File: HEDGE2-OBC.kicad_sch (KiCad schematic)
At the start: 31 parts, among them J1 MMBX-S50-0-18, J2 SQT-110-01-L-D, J3 SMA-J-P-X-RA-TH1, U1 ADP7158ARDZ-3.3-R7

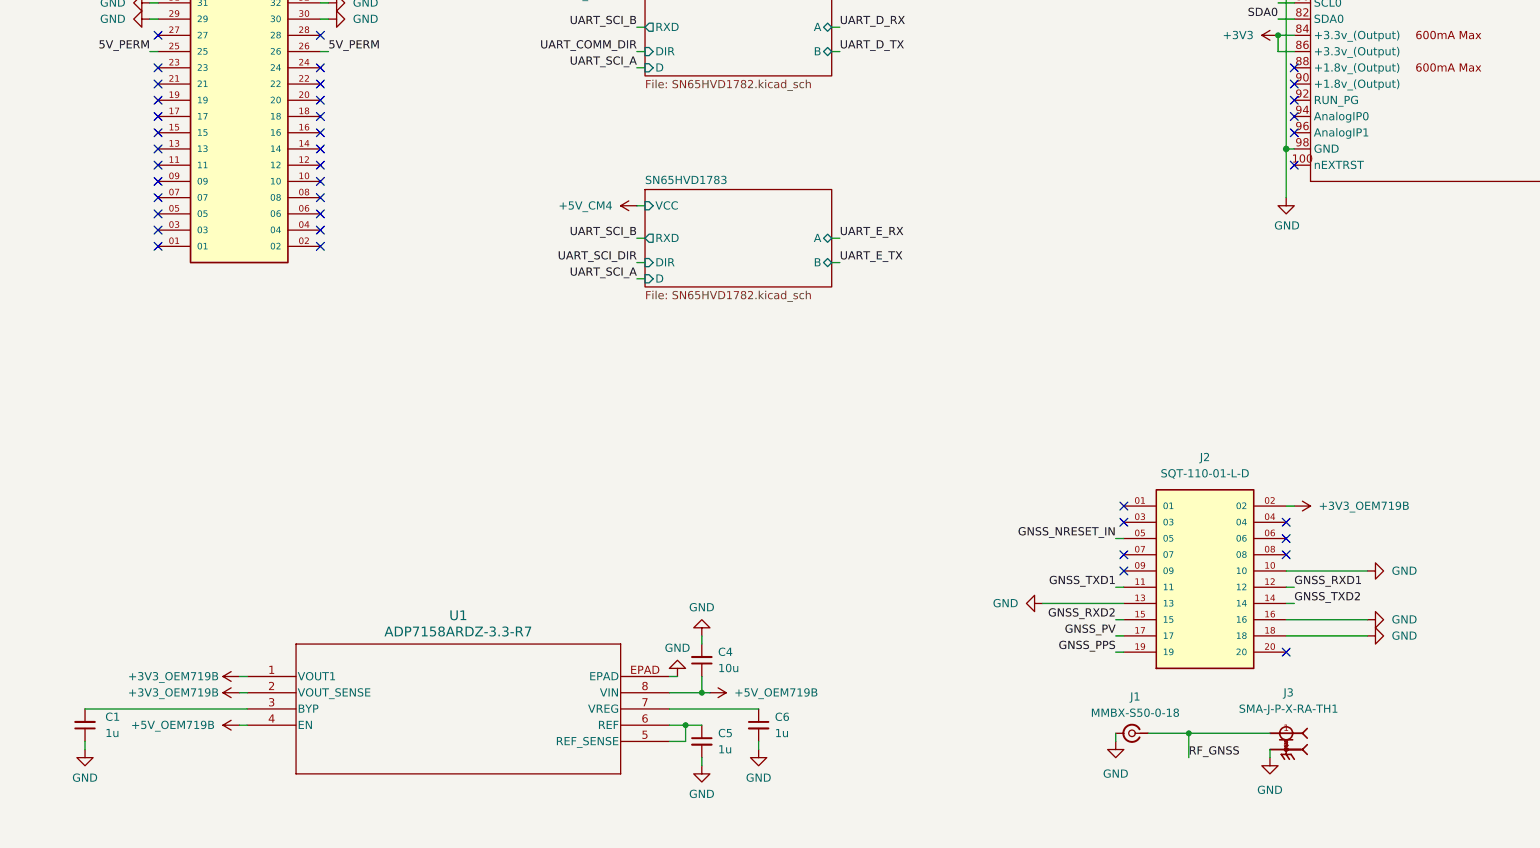
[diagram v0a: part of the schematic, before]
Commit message: Rework Novatel OEM719B symbol and footprint
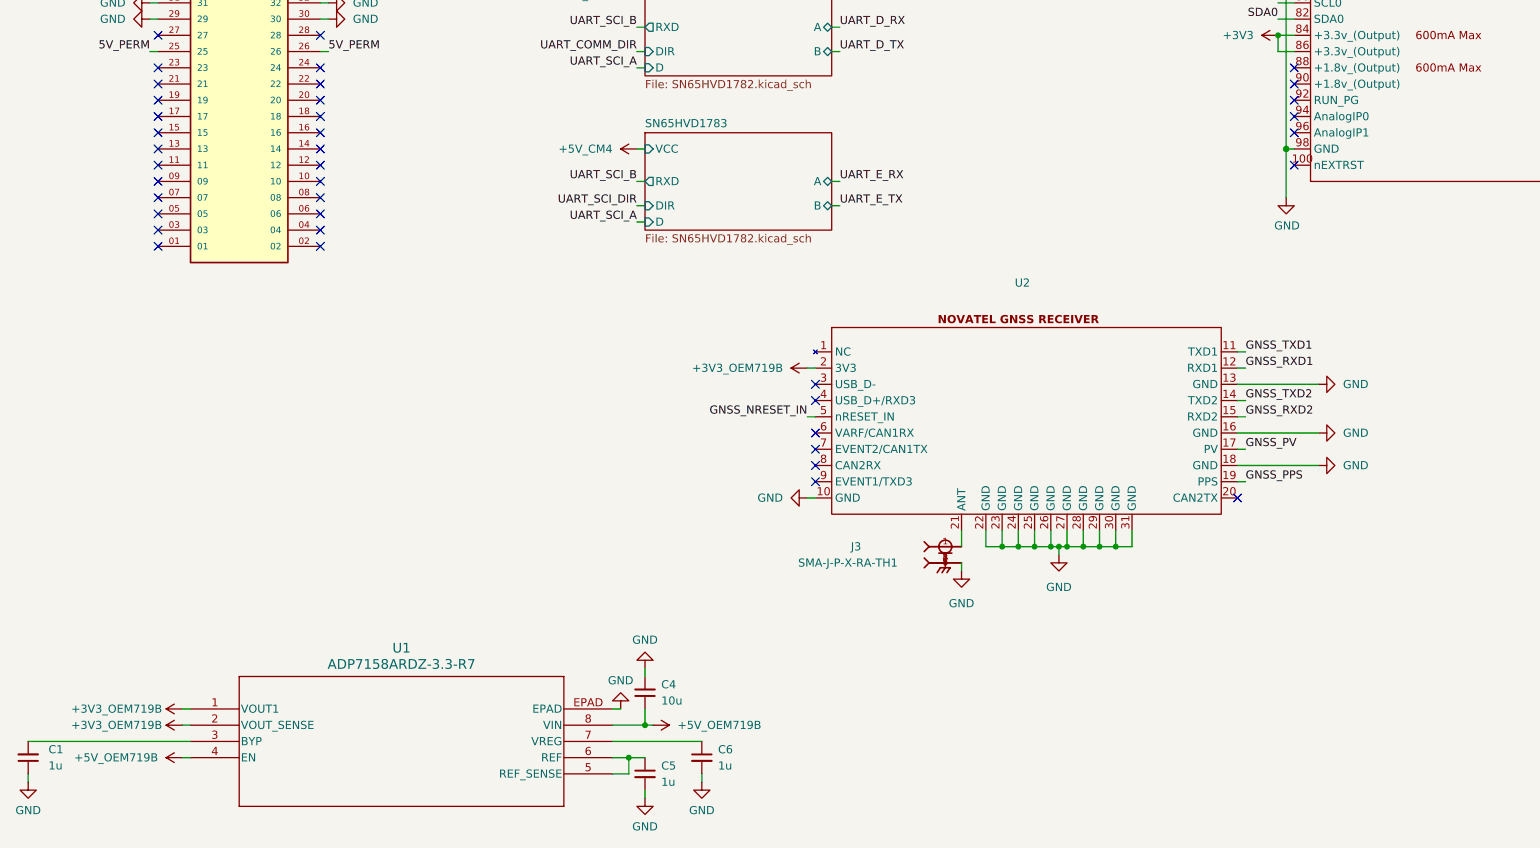
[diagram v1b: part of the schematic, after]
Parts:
- removed J1: MMBX-S50-0-18, Novatel:MMBX-S50-0-18, symbol Novatel:MMBX-S50-0-18
- removed J2: SQT-110-01-L-D, SQT-110-01-L-D:SAMTEC_SQT-110-01-L-D, symbol SQT-110-01-L-D:SQT-110-01-L-D
- added U2: ~, OEM719B:OEM719B, symbol OEM719B:NOVATEL_OEM719
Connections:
- net +3V3_OEM719B: now also U2.2 (3V3)
- net GND: now also U2.10 (GND), U2.13 (GND), U2.16 (GND), U2.18 (GND), U2.22 (GND), U2.23 (GND), U2.24 (GND), U2.25 (GND), U2.26 (GND), U2.27 (GND), U2.28 (GND), U2.29 (GND), U2.30 (GND), U2.31 (GND)
- net GNSS_NRESET_IN: now also U2.5 (nRESET_IN)
- net GNSS_PPS: now also U2.19 (PPS)
- net GNSS_PV: now also U2.17 (PV)
- net GNSS_RXD1: now also U2.12 (RXD1)
- net GNSS_RXD2: now also U2.15 (RXD2)
- net GNSS_TXD1: now also U2.11 (TXD1)
- net GNSS_TXD2: now also U2.14 (TXD2)
- net RF_GNSS: no longer names the net of J3.1
- net RF_GNSS: now also U2.21 (ANT)
- no-connect marks 205 -> 204
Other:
- moved on the sheet: C1, C4, C5, C6, J3, U1

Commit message: Layout PCB; update footprints with 3D models
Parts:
- added C7, C8: 0u1, Capacitor_SMD:C_0805_2012Metric, symbol Device:C_Small
- added R20, R21: 4k7, Resistor_SMD:R_0805_2012Metric, symbol Device:R_Small_US
- added R5: 10k, Resistor_SMD:R_0805_2012Metric, symbol Device:R_Small_US
- added U3: TXS0102QDCURQ1, TXS0102QDCURQ1:SOP50P310X90-8N, symbol TXS0102QDCURQ1:TXS0102QDCURQ1
- renumbered J3 to J1, R9 to R10, R10 to R11, R5 to R6, R6 to R7, R7 to R8, R8 to R9
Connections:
- net +3V3: now also C7.2, U3.3 (VCCA)
- net +5V_MPU: now also C8.1, R20.2, R21.2, U3.7 (VCCB)
- net GND: now also C7.1, C8.2, R5.1, U3.2 (GND)
- net SCL0 renamed SCL0_3V3
- net SCL0_3V3: now also U3.5 (A1)
- net SDA0 renamed SDA0_3V3
- net SDA0_3V3: now also U3.4 (A2)
- new net I2C_EN: R5.2, U3.6 (OE)
- new net SCL0_5V: R20.1, U3.1 (B2)
- new net SDA0_5V: R21.1, U3.8 (B1)
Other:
- moved on the sheet: D1, D2, J1, R10, R11, R8, R9, U2

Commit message: Continue PCB layout
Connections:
- net CAN_A_S: now also Module1.49 (GPIO18); no longer Module1.29 (GPIO16)
- net CAN_B_S: now also Module1.37 (GPIO7); no longer Module1.58 (GPIO2)
- net GNSS_NRESET_IN: now also Module1.48 (GPIO27); no longer Module1.38 (GPIO11)
- net I2C_EN: now also Module1.30 (GPIO6)
- net UART_COMM_DIR: now also Module1.41 (GPIO25); no longer Module1.47 (GPIO23)
- net UART_SCI_A: no longer Module1.39 (GPIO8)
- net UART_SCI_B: no longer Module1.40 (GPIO9)
- net UART_SCI_DIR: now also Module1.26 (GPIO19); no longer Module1.45 (GPIO24)
- new net UART_COMM_A: Module1.39 (GPIO8)
- new net UART_COMM_B: Module1.40 (GPIO9)
- no-connect marks 204 -> 203
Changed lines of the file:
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@@
 	)
 	(no_connect
+		(at 276.86 90.17)
+	)
+	(no_connect
 		(at 38.1 138.43)
 	)
@@
 	)
 	(no_connect
-		(at 215.9 92.71)
-	)
-	(no_connect
 		(at 215.9 110.49)
 	)
@@
 	)
 	(no_connect
-		(at 276.86 95.25)
-	)
-	(no_connect
 		(at 330.2 69.85)
 	)
@@
 	)
 	(no_connect
-		(at 276.86 85.09)
+		(at 276.86 92.71)
 	)
 	(no_connect
@@
 	)
 	(no_connect
+		(at 215.9 80.01)
+	)
+	(no_connect
 		(at 276.86 57.15)
 	)
@@
 	)
 	(no_connect
+		(at 215.9 105.41)
+	)
+	(no_connect
 		(at 38.1 163.83)
 	)
@@
 	)
 	(no_connect
-		(at 215.9 64.77)
-	)
-	(no_connect
 		(at 276.86 156.21)
 	)
@@
 	)
 	(no_connect
+		(at 276.86 69.85)
+	)
+	(no_connect
 		(at 215.9 143.51)
 	)
@@
 	)
 	(no_connect
-		(at 215.9 69.85)
-	)
-	(no_connect
 		(at 330.2 52.07)
 	)
@@
 	)
 	(no_connect
-		(at 276.86 80.01)
-	)
-	(no_connect
 		(at 215.9 46.99)
 	)
@@
 	(wire
 		(pts
+			(xy 213.36 69.85) (xy 215.9 69.85)
+		)
+		(stroke
+			(width 0)
+			(type default)
+		)
+	)
+	(wire
+		(pts
 			(xy 36.83 133.35) (xy 38.1 133.35)
 		)
@@
 	(wire
 		(pts
-			(xy 276.86 90.17) (xy 279.4 90.17)
+			(xy 215.9 64.77) (xy 213.36 64.77)
 		)
 		(stroke
@@
 	(wire
 		(pts
+			(xy 276.86 80.01) (xy 279.4 80.01)
+		)
+		(stroke
+			(width 0)
+			(type default)
+		)
+	)
+	(wire
+		(pts
 			(xy 213.36 100.33) (xy 215.9 100.33)
 		)
@@
 	(wire
 		(pts
+			(xy 276.86 95.25) (xy 279.4 95.25)
+		)
+		(stroke
+			(width 0)
+			(type default)
+		)
+	)
+	(wire
+		(pts
 			(xy 109.22 243.84) (xy 110.49 243.84)
 		)
@@
 	(wire
 		(pts
-			(xy 276.86 92.71) (xy 279.4 92.71)
+			(xy 276.86 85.09) (xy 279.4 85.09)
 		)
 		(stroke
@@
 	(wire
 		(pts
-			(xy 276.86 69.85) (xy 279.4 69.85)
-		)
-		(stroke
-			(width 0)
-			(type solid)
-		)
-	)
-	(wire
-		(pts
 			(xy 327.66 57.15) (xy 327.66 64.77)
 		)
@@
 	(wire
 		(pts
-			(xy 213.36 80.01) (xy 215.9 80.01)
+			(xy 213.36 92.71) (xy 215.9 92.71)
 		)
 		(stroke
@@
 	(wire
 		(pts
-			(xy 213.36 105.41) (xy 215.9 105.41)
-		)
-		(stroke
-			(width 0)
-			(type default)
-		)
-	)
-	(wire
-		(pts
 			(xy 327.66 110.49) (xy 327.66 118.11)
 		)
@@
 				)
 			)
-			(table_cell "GNSS_TXD"
+			(table_cell "GNSS_TXD2"
 				(exclude_from_sim no)
 				(at 264.16 232.41 0)
@@
 				)
 			)
-			(table_cell "GNSS_RXD"
+			(table_cell "GNSS_RXD2"
 				(exclude_from_sim no)
 				(at 264.16 234.95 0)
@@
 		)
 	)
-	(label "UART_SCI_A"
+	(label "UART_COMM_A"
 		(at 279.4 82.55 0)
 		(effects
@@
 		)
 	)
+	(label "I2C_EN"
+		(at 213.36 69.85 180)
+		(effects
+			(font
+				(size 1.27 1.27)
+			)
+			(justify right bottom)
+		)
+	)
 	(label "UART_COMM_DIR"
 		(at 113.03 140.97 180)
@@
 		)
 	)
-	(label "UART_SCI_B"
+	(label "UART_COMM_B"
 		(at 113.03 137.16 180)
 		(effects
@@
 	)
 	(label "CAN_A_S"
-		(at 279.4 69.85 0)
+		(at 279.4 95.25 0)
 		(effects
 			(font
@@
 	)
 	(label "GNSS_NRESET_IN"
-		(at 213.36 80.01 180)
+		(at 213.36 92.71 180)
 		(effects
 			(font
@@
 	)
 	(label "UART_SCI_DIR"
-		(at 279.4 90.17 0)
+		(at 213.36 64.77 180)
 		(effects
 			(font
 				(size 1.27 1.27)
 			)
-			(justify left bottom)
+			(justify right bottom)
 		)
 	)
@@
 	)
 	(label "UART_COMM_DIR"
-		(at 279.4 92.71 0)
+		(at 279.4 85.09 0)
 		(effects
 			(font
@@
 		)
 	)
-	(label "UART_SCI_B"
+	(label "UART_COMM_B"
 		(at 213.36 82.55 180)
 		(effects
@@
 	)
 	(label "CAN_B_S"
-		(at 213.36 105.41 180)
+		(at 279.4 80.01 0)
 		(effects
 			(font
 				(size 1.27 1.27)
 			)
-			(justify right bottom)
+			(justify left bottom)
 		)
 	)
@@
 		)
 	)
-	(label "UART_SCI_A"
+	(label "UART_COMM_A"
 		(at 113.03 143.51 180)
 		(effects

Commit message: Continue layout
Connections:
- net +5V_CM4: now also C8.1, R20.2, R21.2, U3.7 (VCCB)
- net +5V_MPU: no longer C8.1, R20.2, R21.2, U3.7 (VCCB)

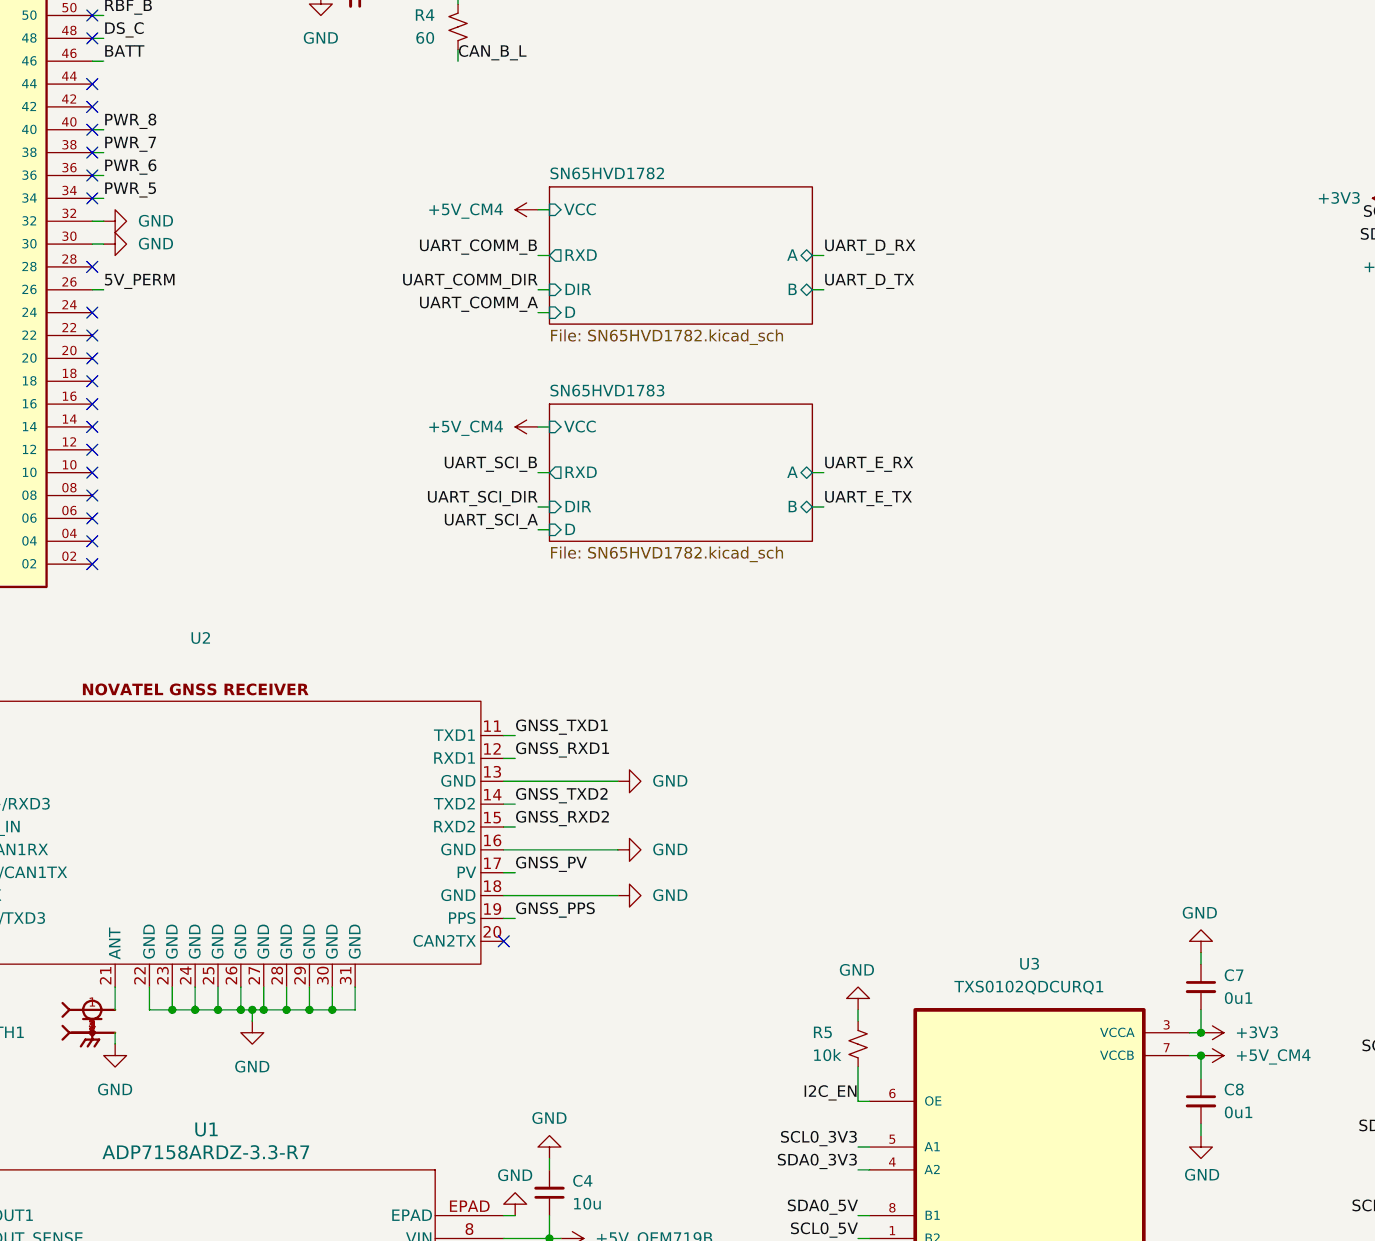
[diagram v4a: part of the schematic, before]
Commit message: Fix MMBX footprint; resolve ERC/DRC
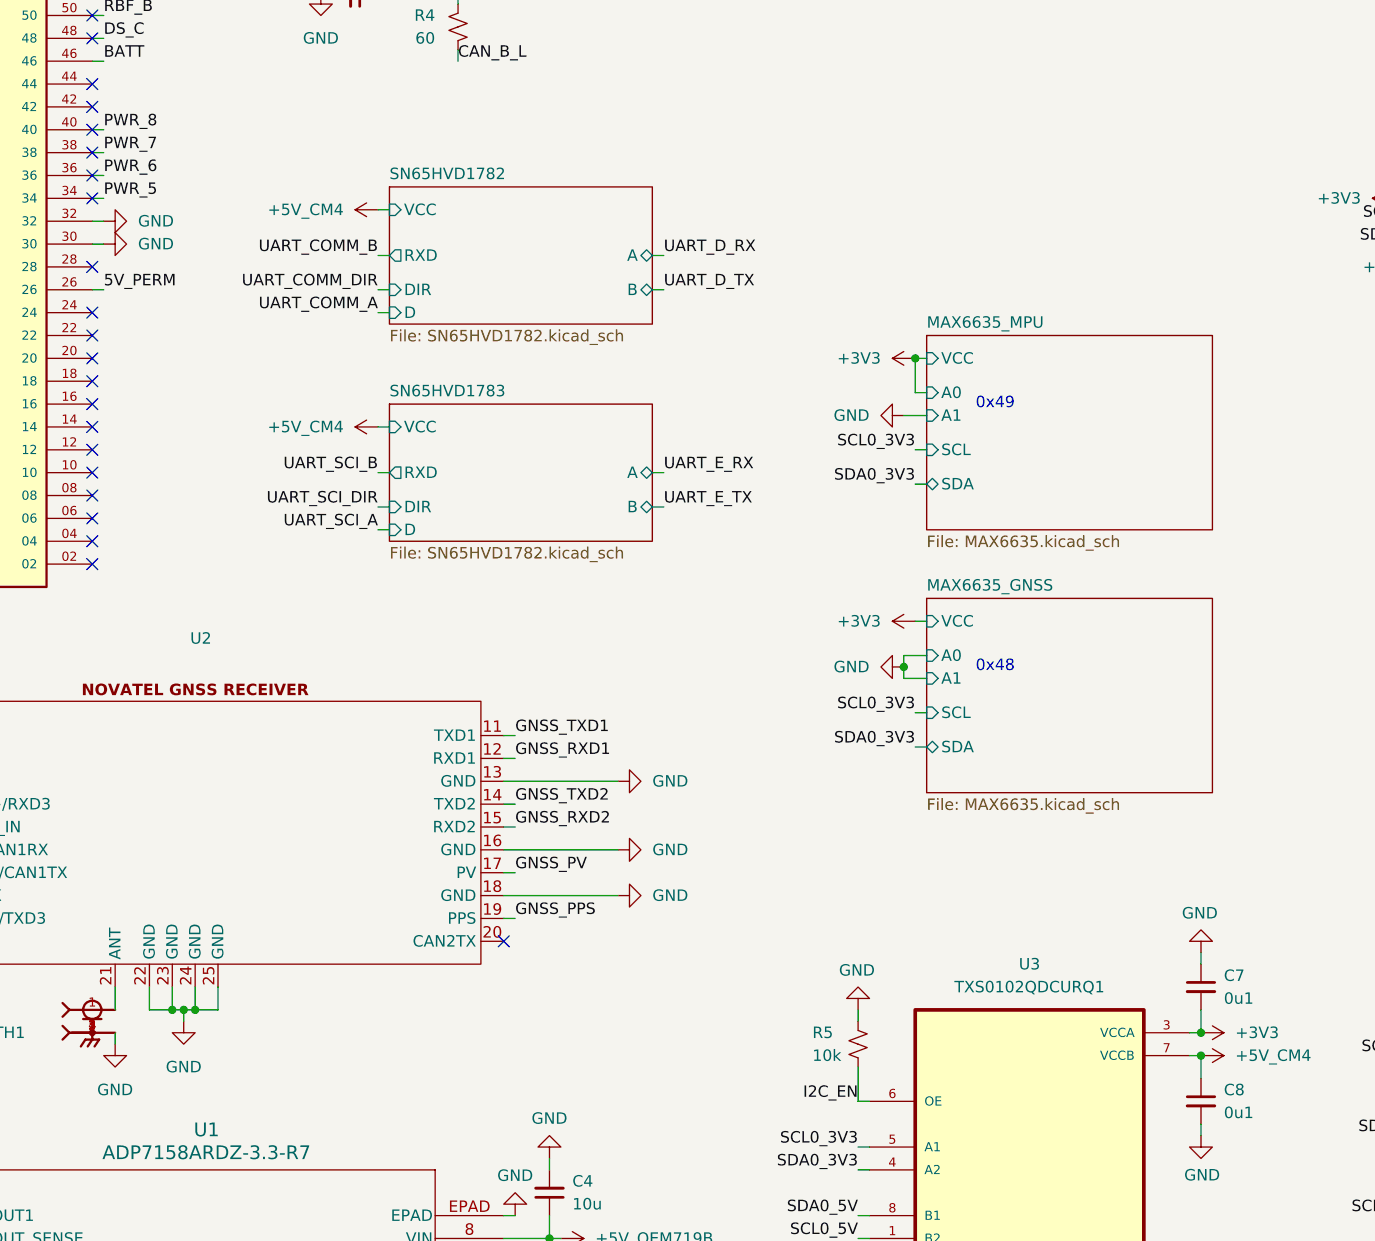
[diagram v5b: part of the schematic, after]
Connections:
- net GND: no longer U2.26 (GND), U2.27 (GND), U2.28 (GND), U2.29 (GND), U2.30 (GND), U2.31 (GND)
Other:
- added sheet MAX6635_GNSS (MAX6635.kicad_sch)
- added sheet MAX6635_MPU (MAX6635.kicad_sch)
- note added: "0x48"
- note added: "0x49"

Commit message: Add functional block labels to schematic
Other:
- note added: "GNSS"
- note added: "Housekeeping (TEMP)"
- note added: "Housekeeping (VOLT/CURR)"
- note added: "I2C0 BUS"
- note added: "RS-485"
- note added: "SPACECRAFT BUS"
- note added: "SpaceCAN (CANbus)"
- moved on the sheet: C2, C3, C7, C8, D1, D2, J1, JP1, JP2, Module1A, Module1B, R1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
